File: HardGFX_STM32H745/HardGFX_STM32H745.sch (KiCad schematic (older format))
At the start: 16 parts, among them SW2 SW_MEC_5E, U1 STM32H745BIT6, X1 XO32, Y1 ECS-.327-6-34R-TR

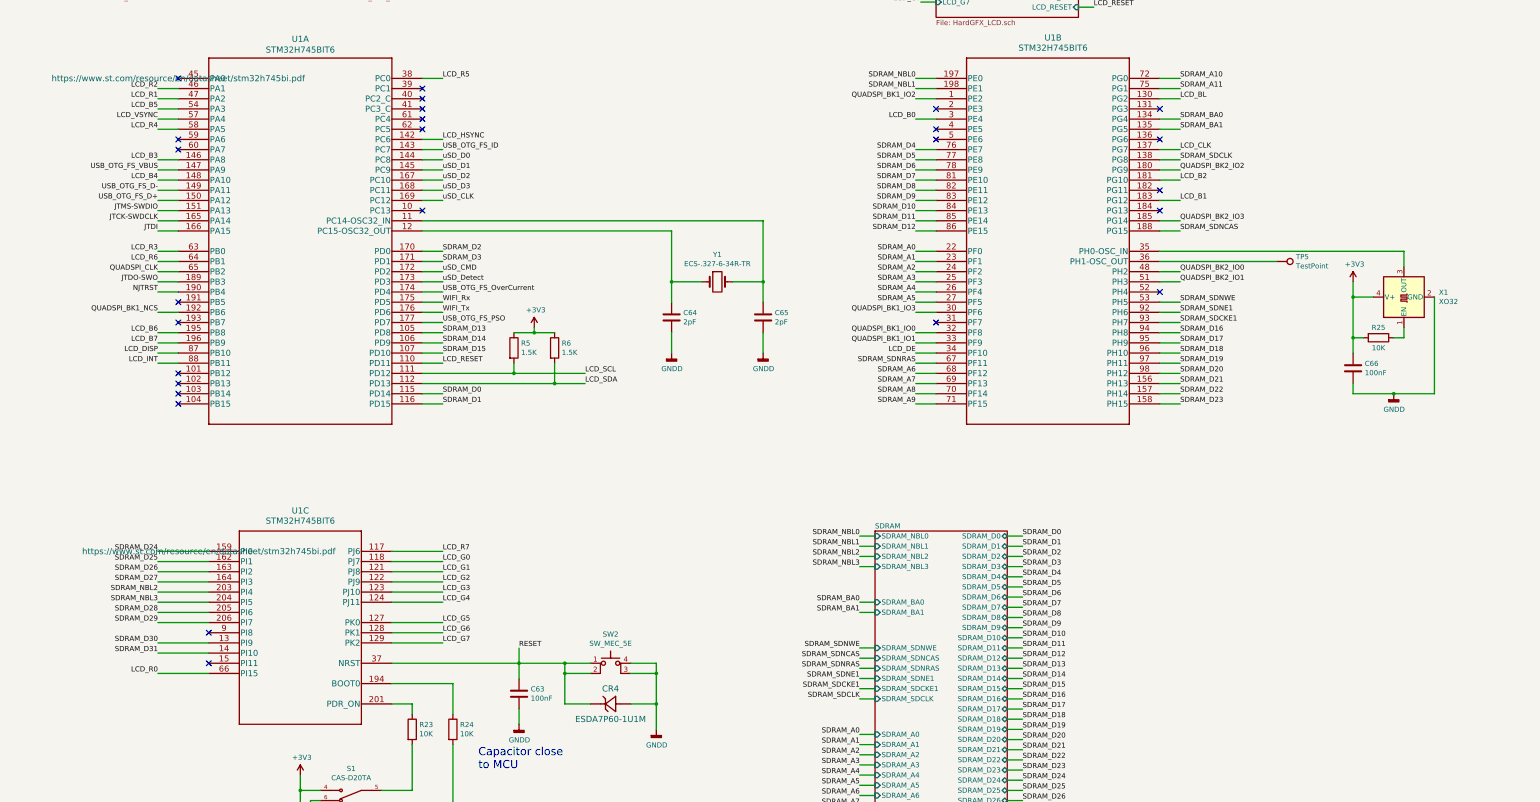
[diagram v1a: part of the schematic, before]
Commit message: Filling field for do BOM with Kicost  and create proyect on IDE to start setting peripheral in MCU
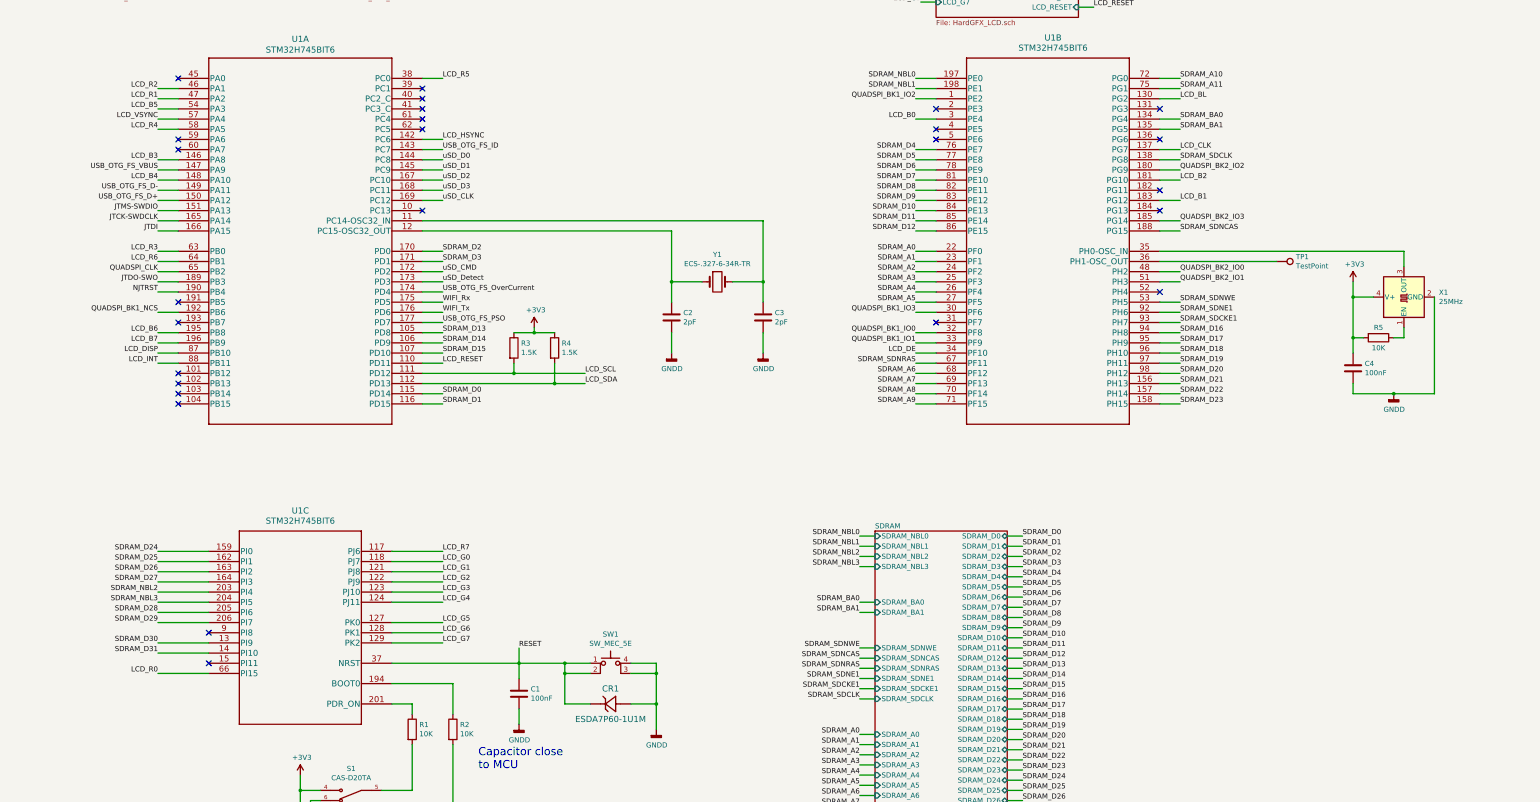
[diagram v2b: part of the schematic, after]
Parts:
- CR1: renamed from CR4; Digikey# (none) -> 497-16253-1-ND; MANUFACTURER (none) -> STMicroelectronics; Manf# (none) -> ESDA7P60-1U1M; Mouser# (none) -> 511-ESDA7P60-1U1M
- S1: Digikey# (none) -> CASD20JCT-ND; Manf# (none) -> CAS-D20TA; Mouser# (none) -> 229-CAS-D20TA
- SW1: renamed from SW2; footprint Button_Switch_SMD:SW_SPST_Omron_B3FS-100xP -> (none); Digikey# (none) -> 732-7022-1-ND; MANUFACTURER (none) -> Wurth Elektronik; Manf# (none) -> 430481025816; Mouser# (none) -> 710-430481025816
- U1: Mouser# (none) -> 511-STM32H745BIT6
- X1: value XO32 -> 25MHz; footprint Oscillator:Oscillator_SMD_EuroQuartz_XO32-4Pin_3.2x2.5mm -> Oscillator:Oscillator_SMD_EuroQuartz_XO32-4Pin_3.2x2.5m; Digikey# (none) -> 50-ECS-2520MVQ-250-BS-CT-ND; MANUFACTURER (none) -> ECS; Manf# (none) -> ECS-2520MVQ-250-BS-TR; Mouser# (none) -> 520-2520MVQ-250-BSTR
- Y1: Digikey# (none) -> 535-12943-1-ND; MANUFACTURER (none) -> ABRACON; Manf# (none) -> ABS07-LR-32.768KHZ-6-1-T; Mouser# (none) -> 815-ABS07LR32.76-61T
- renumbered C63 to C1, C64 to C2, C65 to C3, C66 to C4, R23 to R1, R24 to R2, R5 to R3, R6 to R4, R25 to R5, TP5 to TP1
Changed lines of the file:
@@
 Sheet 1 8
 Title "Main"
-Date "2021-06-19"
+Date "2021-08-23"
 Rev "Rev. 1"
 Comp "HardGFX"
@@
 F 1 "STM32H745BIT6" H 3850 3581 60  0000 C CNN
 F 2 "STM32H745BIT3:STM32H745BIT3" H 3850 3540 60  0001 C CNN
-F 3 "https://www.st.com/resource/en/datasheet/stm32h745bi.pdf" H 2650 3300 60  0000 C CNN
+F 3 "https://www.st.com/resource/en/datasheet/stm32h745bi.pdf" H 2650 3300 60  0001 C CNN
 F 4 "STM32H745BIT6" H 2650 3300 50  0001 C CNN "Manf#"
 F 5 "STM32H745BIT6-ND" H 2650 3300 50  0001 C CNN "Digikey#"
 F 6 "STMicroelectronics" H 2650 3300 50  0001 C CNN "MANUFACTURER"
+F 7 "511-STM32H745BIT6" H 2650 3300 50  0001 C CNN "Mouser#"
 	1    2650 3300
 	1    0    0    -1
@@
 F 1 "STM32H745BIT6" H 3850 8250 60  0000 C CNN
 F 2 "STM32H745BIT3:STM32H745BIT3" H 4150 8190 60  0001 C CNN
-F 3 "https://www.st.com/resource/en/datasheet/stm32h745bi.pdf" H 2950 7950 60  0000 C CNN
+F 3 "https://www.st.com/resource/en/datasheet/stm32h745bi.pdf" H 2950 7950 60  0001 C CNN
 F 4 "STM32H745BIT6" H 2950 7950 50  0001 C CNN "Manf#"
 F 5 "STM32H745BIT6-ND" H 2950 7950 50  0001 C CNN "Digikey#"
 F 6 "STMicroelectronics" H 2950 7950 50  0001 C CNN "MANUFACTURER"
+F 7 "511-STM32H745BIT6" H 2950 7950 50  0001 C CNN "Mouser#"
 	3    2950 7950
 	1    0    0    -1
@@
 	2450 6100 2650 6100
 $Comp
-L Device:R R5
+L Device:R R3
 U 1 1 61531638
 P 5950 5950
-F 0 "R5" H 6020 5996 50  0000 L CNN
+F 0 "R3" H 6020 5996 50  0000 L CNN
 F 1 "1.5K" H 6020 5905 50  0000 L CNN
 F 2 "" V 5880 5950 50  0001 C CNN
@@
 $EndComp
 $Comp
-L Device:R R6
+L Device:R R4
 U 1 1 6153683C
 P 6350 5950
-F 0 "R6" H 6420 5996 50  0000 L CNN
+F 0 "R4" H 6420 5996 50  0000 L CNN
 F 1 "1.5K" H 6420 5905 50  0000 L CNN
 F 2 "" V 6280 5950 50  0001 C CNN
@@
 	6350 6300 6350 6100
 $Comp
-L power:+3V3 #PWR064
+L power:+3V3 #PWR04
 U 1 1 6156DDD9
 P 6150 5750
-F 0 "#PWR064" H 6150 5600 50  0001 C CNN
+F 0 "#PWR04" H 6150 5600 50  0001 C CNN
 F 1 "+3V3" H 6165 5923 50  0000 C CNN
 F 2 "" H 6150 5750 50  0001 C CNN
@@
 F 1 "CAS-D20TA" H 4350 10177 50  0000 C CNN
 F 2 "CAS-D20TA:SW_CAS-D20TA" H 4350 10400 50  0001 L BNN
-F 3 "https://ar.mouser.com/datasheet/2/972/cas-1628136.pdf" H 4350 10400 50  0001 L BNN
+F 3 "https://www.nidec-copal-electronics.com/e/catalog/switch/cas.pdf" H 4350 10400 50  0001 L BNN
 F 4 "N/A" H 4350 10400 50  0001 L BNN "PARTREV"
 F 5 "Nidec" H 4350 10400 50  0001 L BNN "MANUFACTURER"
 F 6 "Manufacturer Recommendations" H 4350 10400 50  0001 L BNN "STANDARD"
 F 7 "2.5 mm" H 4350 10400 50  0001 L BNN "MAXIMUM_PACKAGE_HEIGHT"
+F 8 "CASD20JCT-ND" H 4350 10400 50  0001 C CNN "Digikey#"
+F 9 "CAS-D20TA" H 4350 10400 50  0001 C CNN "Manf#"
+F 10 "229-CAS-D20TA" H 4350 10400 50  0001 C CNN "Mouser#"
 	1    4350 10400
 	-1   0    0    1
 $EndComp
 $Comp
-L Device:R R23
+L Device:R R1
 U 1 1 60D6A091
 P 4950 9700
-F 0 "R23" H 5020 9746 50  0000 L CNN
+F 0 "R1" H 5020 9746 50  0000 L CNN
 F 1 "10K" H 5020 9655 50  0000 L CNN
 F 2 "" V 4880 9700 50  0001 C CNN
@@
 $EndComp
 $Comp
-L Device:R R24
+L Device:R R2
 U 1 1 60D6B53A
 P 5350 9700
-F 0 "R24" H 5420 9746 50  0000 L CNN
+F 0 "R2" H 5420 9746 50  0000 L CNN
 F 1 "10K" H 5420 9655 50  0000 L CNN
 F 2 "" V 5280 9700 50  0001 C CNN
@@
 	5350 9250 4750 9250
 $Comp
-L power:+3V3 #PWR069
+L power:+3V3 #PWR01
 U 1 1 60E0C22B
 P 3850 10150
-F 0 "#PWR069" H 3850 10000 50  0001 C CNN
+F 0 "#PWR01" H 3850 10000 50  0001 C CNN
 F 1 "+3V3" H 3865 10323 50  0000 C CNN
 F 2 "" H 3850 10150 50  0001 C CNN
@@
 $EndComp
 $Comp
-L power:GNDD #PWR070
+L power:GNDD #PWR02
 U 1 1 60E5F9CA
 P 3950 10700
-F 0 "#PWR070" H 3950 10450 50  0001 C CNN
+F 0 "#PWR02" H 3950 10450 50  0001 C CNN
 F 1 "GNDD" H 3954 10545 50  0000 C CNN
 F 2 "" H 3950 10700 50  0001 C CNN
@@
 For default:\n\n* BOOT0 to GNDD \n* PRD_ON to VDD
 $Comp
-L Switch:SW_MEC_5E SW2
+L Switch:SW_MEC_5E SW1
 U 1 1 60F11BFD
 P 6900 9150
-F 0 "SW2" H 6900 9535 50  0000 C CNN
+F 0 "SW1" H 6900 9535 50  0000 C CNN
 F 1 "SW_MEC_5E" H 6900 9444 50  0000 C CNN
-F 2 "Button_Switch_SMD:SW_SPST_Omron_B3FS-100xP" H 6900 9450 50  0001 C CNN
-F 3 "https://ar.mouser.com/datasheet/2/445/midc_s_a0010704869_1-2286593.pdf" H 6900 9450 50  0001 C CNN
+F 2 "" H 6900 9450 50  0001 C CNN
+F 3 "https://www.we-online.com/katalog/datasheet/4304x1xxx8x6.pdf" H 6900 9450 50  0001 C CNN
+F 4 "732-7022-1-ND" H 6900 9150 50  0001 C CNN "Digikey#"
+F 5 "Wurth Elektronik " H 6900 9150 50  0001 C CNN "MANUFACTURER"
+F 6 "430481025816" H 6900 9150 50  0001 C CNN "Manf#"
+F 7 "710-430481025816" H 6900 9150 50  0001 C CNN "Mouser#"
 	1    6900 9150
 	1    0    0    -1
 $EndComp
 $Comp
-L Device:C C63
+L Device:C C1
 U 1 1 60F1937E
 P 6000 9350
-F 0 "C63" H 6115 9396 50  0000 L CNN
+F 0 "C1" H 6115 9396 50  0000 L CNN
 F 1 "100nF" H 6115 9305 50  0000 L CNN
 F 2 "Capacitor_SMD:C_0603_1608Metric" H 6038 9200 50  0001 C CNN
@@
 Connection ~ 6000 9050
 $Comp
-L power:GNDD #PWR071
+L power:GNDD #PWR03
 U 1 1 60F78CA5
 P 6000 9650
-F 0 "#PWR071" H 6000 9400 50  0001 C CNN
+F 0 "#PWR03" H 6000 9400 50  0001 C CNN
 F 1 "GNDD" H 6004 9495 50  0000 C CNN
 F 2 "" H 6000 9650 50  0001 C CNN
@@
 	6000 9500 6000 9650
 $Comp
-L ESDA7P60-1U1M:ESDA7P60-1U1M CR4
+L ESDA7P60-1U1M:ESDA7P60-1U1M CR1
 U 1 1 60FA530F
 P 6700 9450
-F 0 "CR4" H 6900 9600 60  0000 C CNN
+F 0 "CR1" H 6900 9600 60  0000 C CNN
 F 1 "ESDA7P60-1U1M" H 6900 9300 60  0000 C CNN
 F 2 "ESDA7P60-1U1M:ESDA7P60-1U1M" H 6750 9215 60  0001 C CNN
 F 3 "https://www.st.com/resource/en/datasheet/esda7p60-1u1m.pdf" H 6700 9450 60  0001 C CNN
+F 4 "497-16253-1-ND" H 6700 9450 50  0001 C CNN "Digikey#"
+F 5 "STMicroelectronics" H 6700 9450 50  0001 C CNN "MANUFACTURER"
+F 6 "ESDA7P60-1U1M" H 6700 9450 50  0001 C CNN "Manf#"
+F 7 "511-ESDA7P60-1U1M" H 6700 9450 50  0001 C CNN "Mouser#"
 	1    6700 9450
 	1    0    0    -1
 $EndComp
 $Comp
-L power:GNDD #PWR072
+L power:GNDD #PWR05
 U 1 1 610AF5C0
 P 7350 9700
-F 0 "#PWR072" H 7350 9450 50  0001 C CNN
+F 0 "#PWR05" H 7350 9450 50  0001 C CNN
 F 1 "GNDD" H 7354 9545 50  0000 C CNN
 F 2 "" H 7350 9700 50  0001 C CNN
@@
 F 1 "ECS-.327-6-34R-TR" H 7950 5477 50  0000 C CNN
 F 2 "Crystal:Crystal_SMD_3215-2Pin_3.2x1.5mm" H 7950 5300 50  0001 C CNN
-F 3 "~" H 7950 5300 50  0001 C CNN
+F 3 "https://abracon.com/Resonators/ABS07-LR.pdf" H 7950 5300 50  0001 C CNN
+F 4 "535-12943-1-ND" H 7950 5300 50  0001 C CNN "Digikey#"
+F 5 "815-ABS07LR32.76-61T" H 7950 5300 50  0001 C CNN "Mouser#"
+F 6 "ABS07-LR-32.768KHZ-6-1-T" H 7950 5300 50  0001 C CNN "Manf#"
+F 7 "ABRACON" H 7950 5300 50  0001 C CNN "MANUFACTURER"
 	1    7950 5300
 	1    0    0    -1
@@
 P 14700 5450
 F 0 "X1" V 14746 5106 50  0000 R CNN
-F 1 "XO32" V 14655 5106 50  0000 R CNN
-F 2 "Oscillator:Oscillator_SMD_EuroQuartz_XO32-4Pin_3.2x2.5mm" H 15400 5100 50  0001 C CNN
-F 3 "http://cdn-reichelt.de/documents/datenblatt/B400/XO32.pdf" H 14600 5450 50  0001 C CNN
+F 1 "25MHz" V 14655 5106 50  0000 R CNN
+F 2 "Oscillator:Oscillator_SMD_EuroQuartz_XO32-4Pin_3.2x2.5m" H 15400 5100 50  0001 C CNN
+F 3 "https://ecsxtal.com/store/pdf/ECS-2520MVQ.pdf" H 14600 5450 50  0001 C CNN
+F 4 "50-ECS-2520MVQ-250-BS-CT-ND" H 14700 5450 50  0001 C CNN "Digikey#"
+F 5 "ECS-2520MVQ-250-BS-TR" H 14700 5450 50  0001 C CNN "Manf#"
+F 6 "520-2520MVQ-250-BSTR" H 14700 5450 50  0001 C CNN "Mouser#"
+F 7 "ECS" H 14700 5450 50  0001 C CNN "MANUFACTURER"
 	1    14700 5450
 	0    -1   -1   0
@@
 	14700 5000 14700 5150
 $Comp
-L Device:C C64
+L Device:C C2
 U 1 1 60CE6F6F
 P 7500 5650
-F 0 "C64" H 7615 5696 50  0000 L CNN
+F 0 "C2" H 7615 5696 50  0000 L CNN
 F 1 "2pF" H 7615 5605 50  0000 L CNN
 F 2 "" H 7538 5500 50  0001 C CNN
@@
 $EndComp
 $Comp
-L Device:C C65
+L Device:C C3
 U 1 1 60CE7438
 P 8400 5650
-F 0 "C65" H 8515 5696 50  0000 L CNN
+F 0 "C3" H 8515 5696 50  0000 L CNN
 F 1 "2pF" H 8515 5605 50  0000 L CNN
 F 2 "" H 8438 5500 50  0001 C CNN
@@
 $EndComp
 $Comp
-L power:GNDD #PWR073
+L power:GNDD #PWR06
 U 1 1 60D40C43
 P 7500 6000
-F 0 "#PWR073" H 7500 5750 50  0001 C CNN
+F 0 "#PWR06" H 7500 5750 50  0001 C CNN
 F 1 "GNDD" H 7504 5845 50  0000 C CNN
 F 2 "" H 7500 6000 50  0001 C CNN
@@
 $EndComp
 $Comp
-L power:GNDD #PWR074
+L power:GNDD #PWR07
 U 1 1 60D41A79
 P 8400 6000
-F 0 "#PWR074" H 8400 5750 50  0001 C CNN
+F 0 "#PWR07" H 8400 5750 50  0001 C CNN
 F 1 "GNDD" H 8404 5845 50  0000 C CNN
 F 2 "" H 8400 6000 50  0001 C CNN
@@
 	7500 5800 7500 6000
 $Comp
-L Device:C C66
+L Device:C C4
 U 1 1 60E35174
 P 14200 6150
-F 0 "C66" H 14315 6196 50  0000 L CNN
+F 0 "C4" H 14315 6196 50  0000 L CNN
 F 1 "100nF" H 14315 6105 50  0000 L CNN
 F 2 "Capacitor_SMD:C_0603_1608Metric" H 14238 6000 50  0001 C CNN
@@
 $EndComp
 $Comp
-L Device:R R25
+L Device:R R5
 U 1 1 60E35F10
 P 14450 5850
-F 0 "R25" V 14350 5850 50  0000 C CNN
+F 0 "R5" V 14350 5850 50  0000 C CNN
 F 1 "10K" V 14550 5850 50  0000 C CNN
 F 2 "" V 14380 5850 50  0001 C CNN
@@
 Connection ~ 14200 5850
 $Comp
-L power:+3V3 #PWR075
+L power:+3V3 #PWR08
 U 1 1 60EFD763
 P 14200 5300
-F 0 "#PWR075" H 14200 5150 50  0001 C CNN
+F 0 "#PWR08" H 14200 5150 50  0001 C CNN
 F 1 "+3V3" H 14215 5473 50  0000 C CNN
 F 2 "" H 14200 5300 50  0001 C CNN
@@
 Connection ~ 14200 5450
 $Comp
-L power:GNDD #PWR076
+L power:GNDD #PWR09
 U 1 1 60F2AE10
 P 14600 6400
-F 0 "#PWR076" H 14600 6150 50  0001 C CNN
+F 0 "#PWR09" H 14600 6150 50  0001 C CNN
 F 1 "GNDD" H 14604 6245 50  0000 C CNN
 F 2 "" H 14600 6400 50  0001 C CNN
@@
 NoConn ~ 12300 5400
 $Comp
-L Connector:TestPoint TP5
+L Connector:TestPoint TP1
 U 1 1 6156572C
 P 13450 5100
-F 0 "TP5" V 13404 5288 50  0000 L CNN
+F 0 "TP1" V 13404 5288 50  0000 L CNN
 F 1 "TestPoint" V 13495 5288 50  0000 L CNN
 F 2 "TestPoint:TestPoint_Pad_D1.0mm" H 13650 5100 50  0001 C CNN
@@
 F 5 "STM32H745BIT6-ND" H 10100 3300 50  0001 C CNN "Digikey#"
 F 6 "STMicroelectronics" H 10100 3300 50  0001 C CNN "MANUFACTURER"
+F 7 "511-STM32H745BIT6" H 10100 3300 50  0001 C CNN "Mouser#"
 	2    10100 3300
 	1    0    0    -1

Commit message: I filled more component to Kicost script
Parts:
- TP1: Digikey# (none) -> -; MANUFACTURER (none) -> -; Manf# (none) -> -; Mouser# (none) -> -
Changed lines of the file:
@@
 Sheet 1 8
 Title "Main"
-Date "2021-08-23"
+Date "2021-08-24"
 Rev "Rev. 1"
 Comp "HardGFX"
@@
 F 2 "TestPoint:TestPoint_Pad_D1.0mm" H 13650 5100 50  0001 C CNN
 F 3 "~" H 13650 5100 50  0001 C CNN
+F 4 "-" H 13450 5100 50  0001 C CNN "Digikey#"
+F 5 "-" H 13450 5100 50  0001 C CNN "MANUFACTURER"
+F 6 "-" H 13450 5100 50  0001 C CNN "Manf#"
+F 7 "-" H 13450 5100 50  0001 C CNN "Mouser#"
 	1    13450 5100
 	0    1    1    0

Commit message: Almost I end to fill Kicost field on schematics.
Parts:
- C1, C4: Digikey# (none) -> 311-1088-1-ND; MANUFACTURER (none) -> YAGEO; Manf# (none) -> CC0603KRX7R7BB104; Mouser# (none) -> 603-CC603KRX7R7BB104
- C2, C3: value 2pF -> 1.5pF; Digikey# (none) -> 311-1050-1-ND; MANUFACTURER (none) -> YAGEO; Manf# (none) -> CC0603CRNPO9BN1R5; Mouser# (none) -> 603-CC603CRNPO9BN1R5
- R1, R2, R5: Digikey# (none) -> 311-10.0KHRCT-ND; MANUFACTURER (none) -> YAGEO; Manf# (none) -> RC0603FR-0710KL; Mouser# (none) -> 603-RC0603FR-0710KL
- R3, R4: Digikey# (none) -> 311-1.50KHRCT-ND; MANUFACTURER (none) -> YAGEO; Manf# (none) -> RC0603FR-071K5L; Mouser# (none) -> 603-RC0603FR-071K5L
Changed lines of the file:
@@
 Sheet 1 8
 Title "Main"
-Date "2021-08-24"
+Date "2021-08-25"
 Rev "Rev. 1"
 Comp "HardGFX"
@@
 F 1 "1.5K" H 6020 5905 50  0000 L CNN
 F 2 "" V 5880 5950 50  0001 C CNN
-F 3 "~" H 5950 5950 50  0001 C CNN
+F 3 "https://www.yageo.com/upload/media/product/productsearch/datasheet/rchip/PYu-RC_Group_51_RoHS_L_11.pdf" H 5950 5950 50  0001 C CNN
+F 4 "311-1.50KHRCT-ND" H 5950 5950 50  0001 C CNN "Digikey#"
+F 5 "YAGEO" H 5950 5950 50  0001 C CNN "MANUFACTURER"
+F 6 "RC0603FR-071K5L" H 5950 5950 50  0001 C CNN "Manf#"
+F 7 "603-RC0603FR-071K5L" H 5950 5950 50  0001 C CNN "Mouser#"
 	1    5950 5950
 	1    0    0    -1
@@
 F 1 "1.5K" H 6420 5905 50  0000 L CNN
 F 2 "" V 6280 5950 50  0001 C CNN
-F 3 "~" H 6350 5950 50  0001 C CNN
+F 3 "https://www.yageo.com/upload/media/product/productsearch/datasheet/rchip/PYu-RC_Group_51_RoHS_L_11.pdf" H 6350 5950 50  0001 C CNN
+F 4 "311-1.50KHRCT-ND" H 6350 5950 50  0001 C CNN "Digikey#"
+F 5 "YAGEO" H 6350 5950 50  0001 C CNN "MANUFACTURER"
+F 6 "RC0603FR-071K5L" H 6350 5950 50  0001 C CNN "Manf#"
+F 7 "603-RC0603FR-071K5L" H 6350 5950 50  0001 C CNN "Mouser#"
 	1    6350 5950
 	1    0    0    -1
@@
 F 1 "10K" H 5020 9655 50  0000 L CNN
 F 2 "" V 4880 9700 50  0001 C CNN
-F 3 "~" H 4950 9700 50  0001 C CNN
+F 3 "https://www.yageo.com/upload/media/product/productsearch/datasheet/rchip/PYu-RC_Group_51_RoHS_L_11.pdf" H 4950 9700 50  0001 C CNN
+F 4 "311-10.0KHRCT-ND" H 4950 9700 50  0001 C CNN "Digikey#"
+F 5 "YAGEO" H 4950 9700 50  0001 C CNN "MANUFACTURER"
+F 6 "RC0603FR-0710KL" H 4950 9700 50  0001 C CNN "Manf#"
+F 7 "603-RC0603FR-0710KL" H 4950 9700 50  0001 C CNN "Mouser#"
 	1    4950 9700
 	1    0    0    -1
@@
 F 1 "10K" H 5420 9655 50  0000 L CNN
 F 2 "" V 5280 9700 50  0001 C CNN
-F 3 "~" H 5350 9700 50  0001 C CNN
+F 3 "https://www.yageo.com/upload/media/product/productsearch/datasheet/rchip/PYu-RC_Group_51_RoHS_L_11.pdf" H 5350 9700 50  0001 C CNN
+F 4 "311-10.0KHRCT-ND" H 5350 9700 50  0001 C CNN "Digikey#"
+F 5 "YAGEO" H 5350 9700 50  0001 C CNN "MANUFACTURER"
+F 6 "RC0603FR-0710KL" H 5350 9700 50  0001 C CNN "Manf#"
+F 7 "603-RC0603FR-0710KL" H 5350 9700 50  0001 C CNN "Mouser#"
 	1    5350 9700
 	1    0    0    -1
@@
 F 1 "100nF" H 6115 9305 50  0000 L CNN
 F 2 "Capacitor_SMD:C_0603_1608Metric" H 6038 9200 50  0001 C CNN
-F 3 "https://ar.mouser.com/datasheet/2/447/UPY_GPHC_X7R_6_3V_to_50V_20-1995650.pdf" H 6000 9350 50  0001 C CNN
+F 3 "https://www.yageo.com/upload/media/product/productsearch/datasheet/mlcc/UPY-GPHC_X7R_6.3V-to-50V_18.pdf" H 6000 9350 50  0001 C CNN
+F 4 "311-1088-1-ND" H 6000 9350 50  0001 C CNN "Digikey#"
+F 5 "YAGEO" H 6000 9350 50  0001 C CNN "MANUFACTURER"
+F 6 "CC0603KRX7R7BB104" H 6000 9350 50  0001 C CNN "Manf#"
+F 7 "603-CC603KRX7R7BB104" H 6000 9350 50  0001 C CNN "Mouser#"
 	1    6000 9350
 	1    0    0    -1
@@
 P 7500 5650
 F 0 "C2" H 7615 5696 50  0000 L CNN
-F 1 "2pF" H 7615 5605 50  0000 L CNN
+F 1 "1.5pF" H 7615 5605 50  0000 L CNN
 F 2 "" H 7538 5500 50  0001 C CNN
-F 3 "~" H 7500 5650 50  0001 C CNN
+F 3 "https://www.yageo.com/upload/media/product/productsearch/datasheet/mlcc/UPY-GP_NP0_16V-to-50V_18.pdf" H 7500 5650 50  0001 C CNN
+F 4 "311-1050-1-ND" H 7500 5650 50  0001 C CNN "Digikey#"
+F 5 "YAGEO" H 7500 5650 50  0001 C CNN "MANUFACTURER"
+F 6 "CC0603CRNPO9BN1R5" H 7500 5650 50  0001 C CNN "Manf#"
+F 7 "603-CC603CRNPO9BN1R5" H 7500 5650 50  0001 C CNN "Mouser#"
 	1    7500 5650
 	1    0    0    -1
@@
 P 8400 5650
 F 0 "C3" H 8515 5696 50  0000 L CNN
-F 1 "2pF" H 8515 5605 50  0000 L CNN
+F 1 "1.5pF" H 8515 5605 50  0000 L CNN
 F 2 "" H 8438 5500 50  0001 C CNN
-F 3 "~" H 8400 5650 50  0001 C CNN
+F 3 "https://www.yageo.com/upload/media/product/productsearch/datasheet/mlcc/UPY-GP_NP0_16V-to-50V_18.pdf" H 8400 5650 50  0001 C CNN
+F 4 "311-1050-1-ND" H 8400 5650 50  0001 C CNN "Digikey#"
+F 5 "YAGEO" H 8400 5650 50  0001 C CNN "MANUFACTURER"
+F 6 "CC0603CRNPO9BN1R5" H 8400 5650 50  0001 C CNN "Manf#"
+F 7 "603-CC603CRNPO9BN1R5" H 8400 5650 50  0001 C CNN "Mouser#"
 	1    8400 5650
 	1    0    0    -1
@@
 F 1 "100nF" H 14315 6105 50  0000 L CNN
 F 2 "Capacitor_SMD:C_0603_1608Metric" H 14238 6000 50  0001 C CNN
-F 3 "https://ar.mouser.com/datasheet/2/447/UPY_GPHC_X7R_6_3V_to_50V_20-1995650.pdf" H 14200 6150 50  0001 C CNN
+F 3 "https://www.yageo.com/upload/media/product/productsearch/datasheet/mlcc/UPY-GPHC_X7R_6.3V-to-50V_18.pdf" H 14200 6150 50  0001 C CNN
+F 4 "311-1088-1-ND" H 14200 6150 50  0001 C CNN "Digikey#"
+F 5 "YAGEO" H 14200 6150 50  0001 C CNN "MANUFACTURER"
+F 6 "CC0603KRX7R7BB104" H 14200 6150 50  0001 C CNN "Manf#"
+F 7 "603-CC603KRX7R7BB104" H 14200 6150 50  0001 C CNN "Mouser#"
 	1    14200 6150
 	1    0    0    -1
@@
 F 1 "10K" V 14550 5850 50  0000 C CNN
 F 2 "" V 14380 5850 50  0001 C CNN
-F 3 "~" H 14450 5850 50  0001 C CNN
+F 3 "https://www.yageo.com/upload/media/product/productsearch/datasheet/rchip/PYu-RC_Group_51_RoHS_L_11.pdf" H 14450 5850 50  0001 C CNN
+F 4 "311-10.0KHRCT-ND" H 14450 5850 50  0001 C CNN "Digikey#"
+F 5 "YAGEO" H 14450 5850 50  0001 C CNN "MANUFACTURER"
+F 6 "RC0603FR-0710KL" H 14450 5850 50  0001 C CNN "Manf#"
+F 7 "603-RC0603FR-0710KL" H 14450 5850 50  0001 C CNN "Mouser#"
 	1    14450 5850
 	0    1    1    0
@@
 F 1 "TestPoint" V 13495 5288 50  0000 L CNN
 F 2 "TestPoint:TestPoint_Pad_D1.0mm" H 13650 5100 50  0001 C CNN
-F 3 "~" H 13650 5100 50  0001 C CNN
+F 3 "-" H 13650 5100 50  0001 C CNN
 F 4 "-" H 13450 5100 50  0001 C CNN "Digikey#"
 F 5 "-" H 13450 5100 50  0001 C CNN "MANUFACTURER"
